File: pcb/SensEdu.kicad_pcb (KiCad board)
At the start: 4 copper layers, 99.1 x 54 mm, 147 parts, among them J1 Power, J10 Barrel_Jack_Switch, J11 Conn_01x04_Pin, J12 Conn_01x04_Pin, J13 Conn_02x01, J14 Conn_02x01, J15 Conn_02x01, J16 Conn_02x01, J17 Conn_03x01, J18 Conn_03x01, J19 Conn_03x01, J2 PWM, J20 Conn_01x04_Pin, J3 Analog, J4 PWM, J5 Analog, J6 Communication, J7 Digital, J8 Conn_03x01, J9 Conn_01x04_Pin, U1 AD8426ACPZ-R7, U12 TLS850C2TE_V33, U13 NCP1117-2.5_SOT223, U2 AD8426ACPZ-R7, U3 LT1790ACS6-1.25, U4 R_8_ADI, U5 AD8426ACPZ-R7, U6 AD8426ACPZ-R7, U7 R_8_ADI, U8 DPS310XTSA1

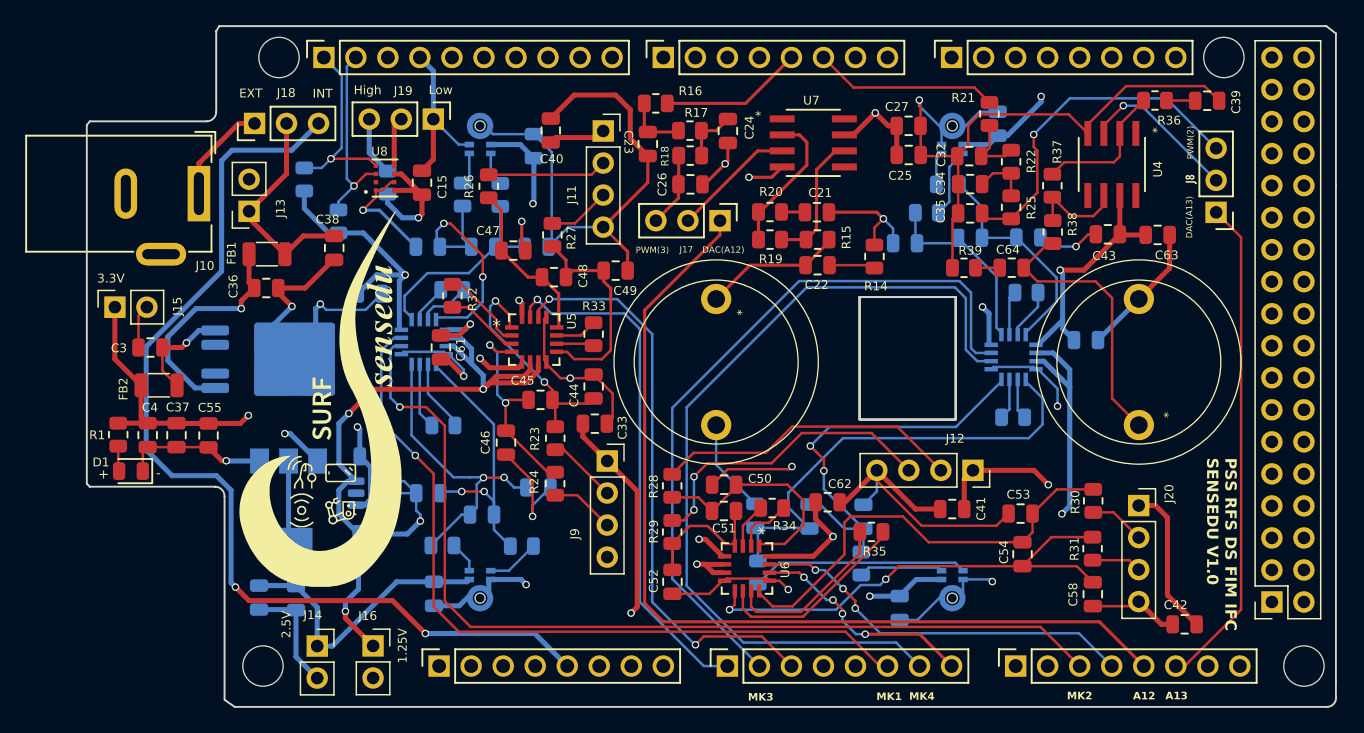
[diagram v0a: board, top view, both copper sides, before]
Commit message: feat: Fix DRC errors and warnings
Updated footprint links
Updated schematic symbol for LT1790 to remove warnings
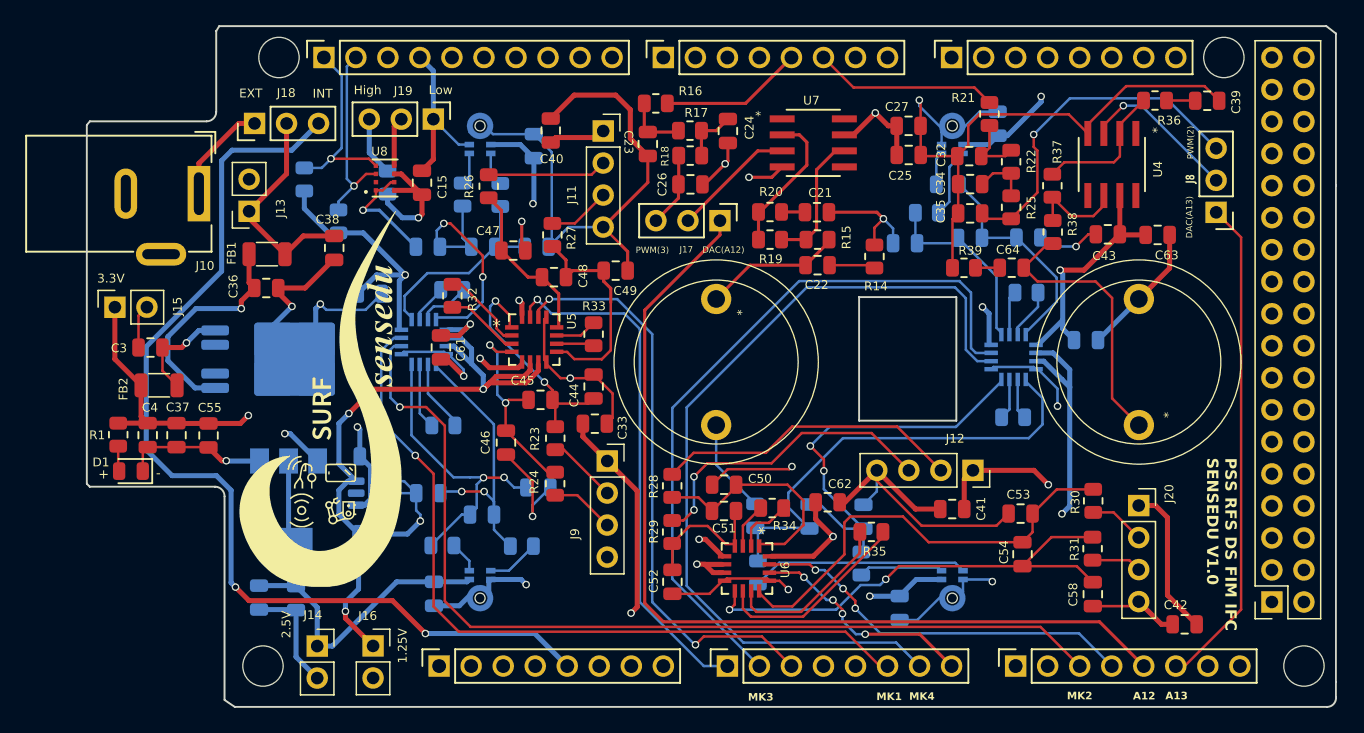
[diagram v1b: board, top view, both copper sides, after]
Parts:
- LS1, LS2: value Speaker_Ultrasound -> 328ST16M
- U4, U7: value R_8_ADI -> ADA4891
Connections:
- U3 pad 3: (no net) -> unconnected-(U3-DNC-Pad3)
- U3 pad 5: (no net) -> unconnected-(U3-DNC-Pad5)
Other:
- outline, holes or cut-outs redrawn

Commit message: feat: fix DRC and ERC errors and warnings
first clean version
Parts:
- removed J17, J18, J8: Conn_03x01, Connector_PinHeader_2.54mm:PinHeader_1x03_P2.54mm_Vertical
- added JP1: Jumper_3_Bridged12, Connector_PinHeader_2.54mm:PinHeader_1x03_P2.54mm_Vertical, F.Cu at (189.6, 61.5)
- added JP2: Jumper_3_Bridged12, Connector_PinHeader_2.54mm:PinHeader_1x03_P2.54mm_Vertical, F.Cu at (150.2, 62.1)
- added JP3: Jumper_3_Bridged12, Connector_PinHeader_2.54mm:PinHeader_1x03_P2.54mm_Vertical, F.Cu at (113.3, 54.1)
- FB1, FB2: footprint Inductor_SMD:L_1206_3216Metric12 -> Inductor_SMD:L_1206_3216Metric
- MK1, MK2, MK3, MK4: footprint IM73A135V01XTSA1:MIC_IM73A135V01XTSA1 -> SensEdu:MIC_IM73A135V01XTSA1
- U1, U2, U5, U6: footprint AD8426:QFN65P400X400X100-16N -> SensEdu:QFN65P400X400X100-16N
- U4, U7: footprint ADA4891-ARZ:ADA4891-1ARZ -> SensEdu:ADA4891-1ARZ
- U8: footprint DPS310XTSA1:XDCR_DPS310XTSA1 -> SensEdu:XDCR_DPS310XTSA1
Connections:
- net /*44 renamed /44*
- net /*45 renamed /45*
- net /*46 renamed /46*
- net /*52 renamed /52*
- net /A11 renamed /Microphones/MIC7_OUT
- net /A14 renamed /CANRX
- net /A15 renamed /CANTX
- net /~{RESET} renamed /~RESET
- J1 pad 1: unconnected-(J1-Pin_1-Pad1) -> /NC
- J1 pad 4: unconnected-(J1-Pin_4-Pad4) -> /3V3
- J5 pad 1: unconnected-(J5-Pin_1-Pad1) -> /A8
- J5 pad 2: unconnected-(J5-Pin_2-Pad2) -> /A9

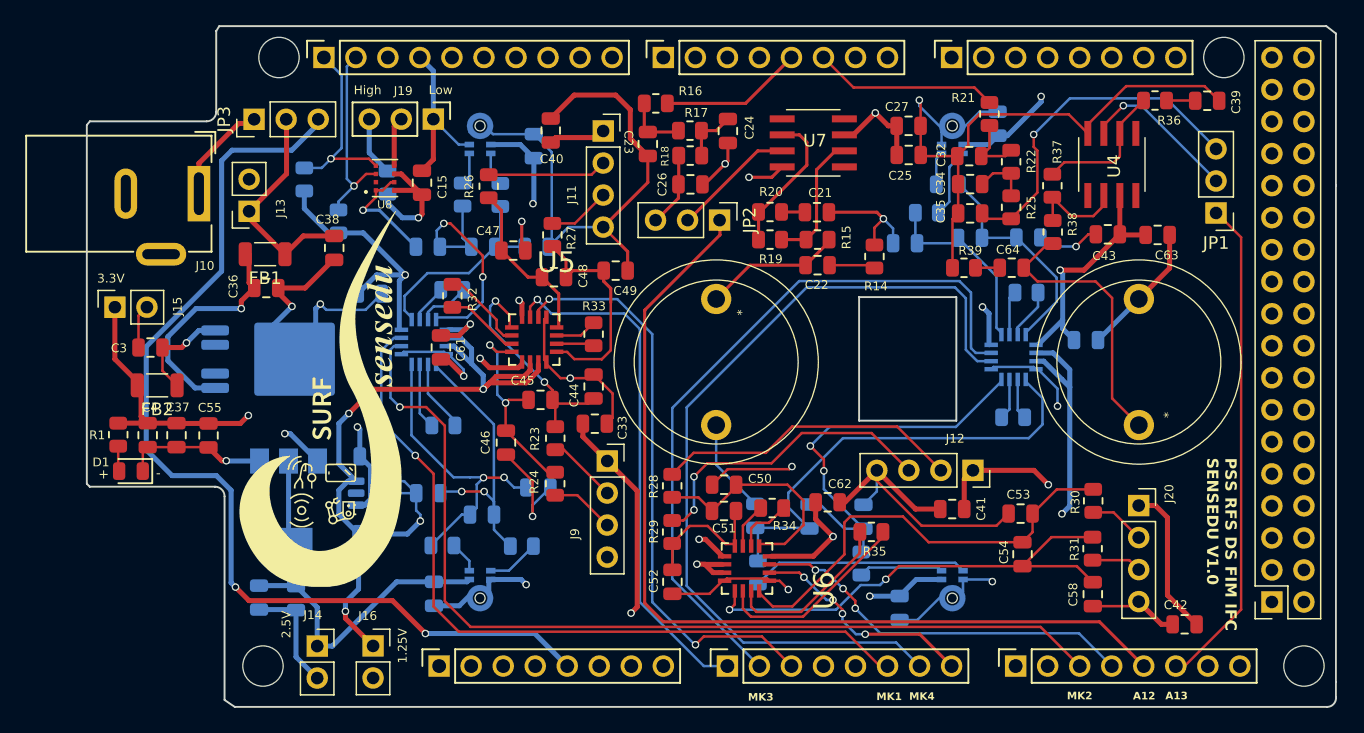
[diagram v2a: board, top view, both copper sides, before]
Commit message: feat: PCB Cleanup and Reorganization
Fixing Project Library Structure
Footprint library
Symbol library
3D Models
Component Datasheets
ERC and DRC error and warning fixes
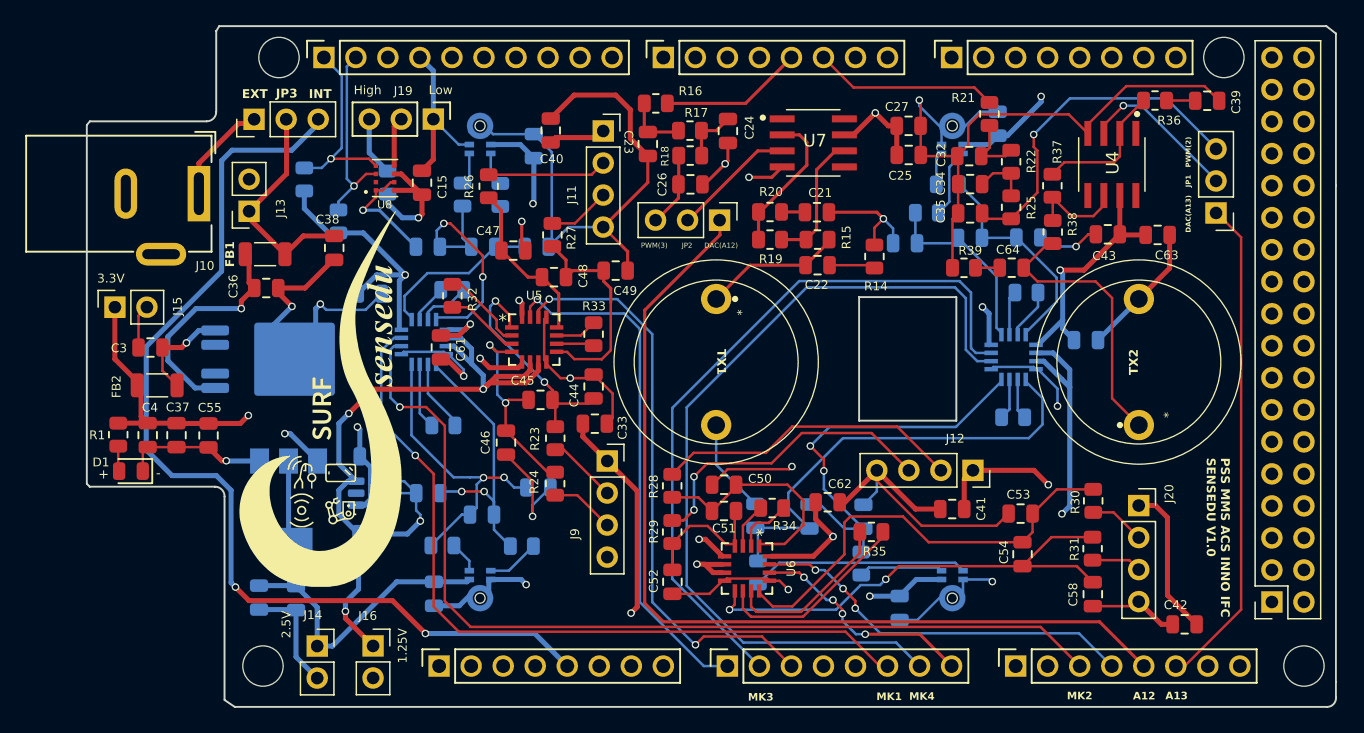
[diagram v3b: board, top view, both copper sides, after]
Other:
- board text added: "DAC(A12)"
- board text added: "DAC(A13)"
- board text added: "EXT"
- board text added: "INT"
- board text added: "PSS MMS ACS INNO IFC SENSEDU V1.0"
- board text added: "PWM(2)"
- board text added: "PWM(3)"
- board text removed: "PSS RFS DS FIM IFC SENSEDU V1.0"

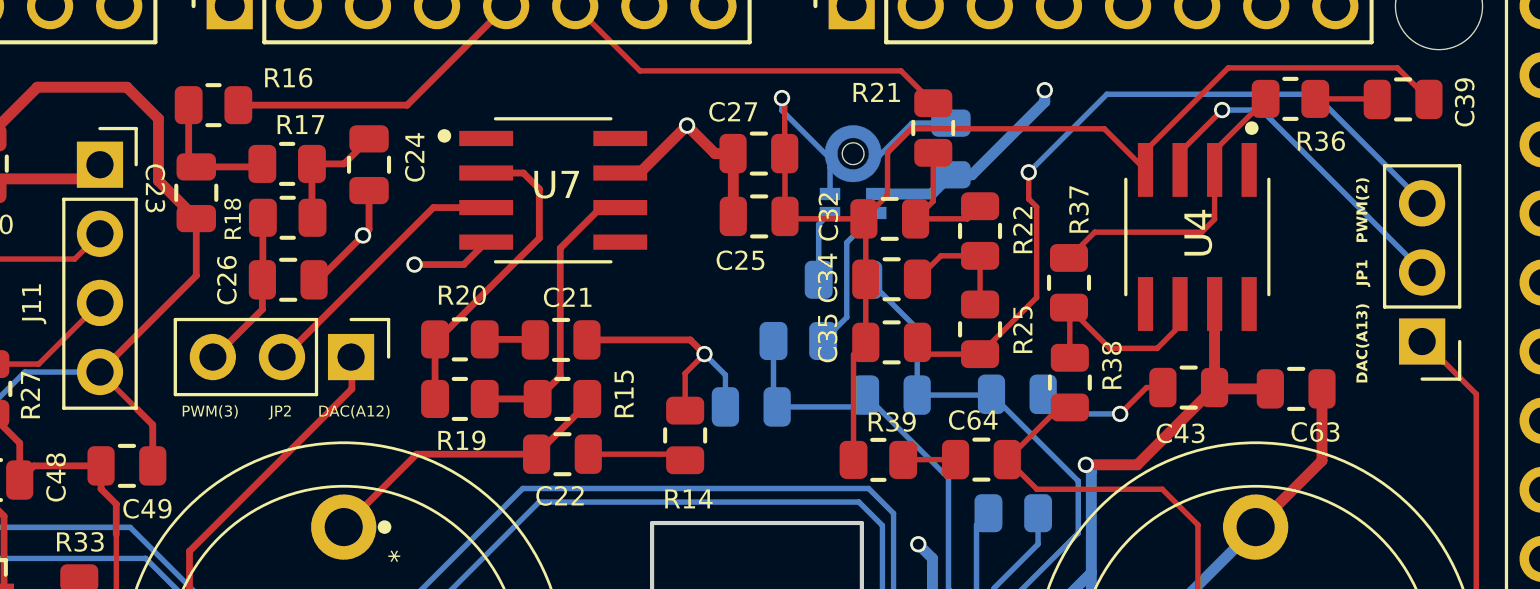
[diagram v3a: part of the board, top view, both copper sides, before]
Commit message: feat: Polished Sensedu schematics
Renamed Sheets
Added Nets
Repaired connections
Renamed Datasheets
Generated new schematic PDF
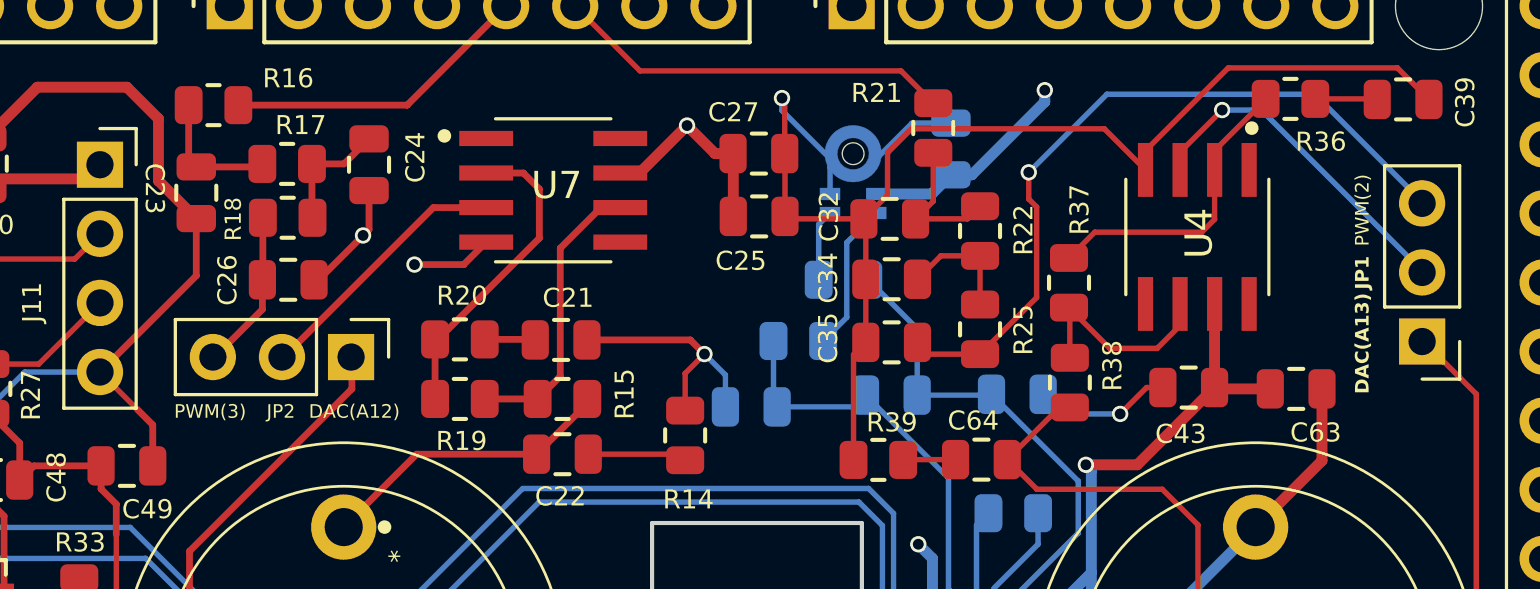
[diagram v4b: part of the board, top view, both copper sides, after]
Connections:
- net Net-(J1-Pin_5) renamed /5V0
- net Net-(U1-+IN1) renamed /Microphones/mic1_out2
- net Net-(U1-+IN2) renamed /Microphones/mic2_out2
- net Net-(U1--IN1) renamed /Microphones/mic1_out1
- net Net-(U1--IN2) renamed /Microphones/mic2_out1
- net Net-(U2-+IN1) renamed /Microphones/mic3_out2
- net Net-(U2-+IN2) renamed /Microphones/mic4_out2
- net Net-(U2--IN1) renamed /Microphones/mic3_out1
- net Net-(U2--IN2) renamed /Microphones/mic4_out1
- net Net-(U5-+IN1) renamed /Microphones/External Microphone Connectors/mic5_out2
- net Net-(U5-+IN2) renamed /Microphones/External Microphone Connectors/mic6_out2
- net Net-(U5--IN1) renamed /Microphones/External Microphone Connectors/mic5_out1
- net Net-(U5--IN2) renamed /Microphones/External Microphone Connectors/mic6_out1
- net Net-(U6-+IN1) renamed /Microphones/External Microphone Connectors/mic7_out2
- net Net-(U6-+IN2) renamed /Microphones/External Microphone Connectors/mic8_out2
- net Net-(U6--IN1) renamed /Microphones/External Microphone Connectors/mic7_out1
- net Net-(U6--IN2) renamed /Microphones/External Microphone Connectors/mic8_out1

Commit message: refactor: Edit speaker/mic symbols and polish
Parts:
- C25: value 1u -> 100n
- C27: value 100n -> 1u
